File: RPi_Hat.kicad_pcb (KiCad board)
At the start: 2 copper layers, 65 x 56 mm, 29 parts, among them J1 CONN_02X19, J10 CONN_01X04, J2 RPi_GPIO, J3 CONN_02X06, J4 CONN_02X06, J5 CONN_02X06, J6 CONN_02X10, J7 CONN_02X10, J8 CONN_02X10, J9 CONN_01X04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

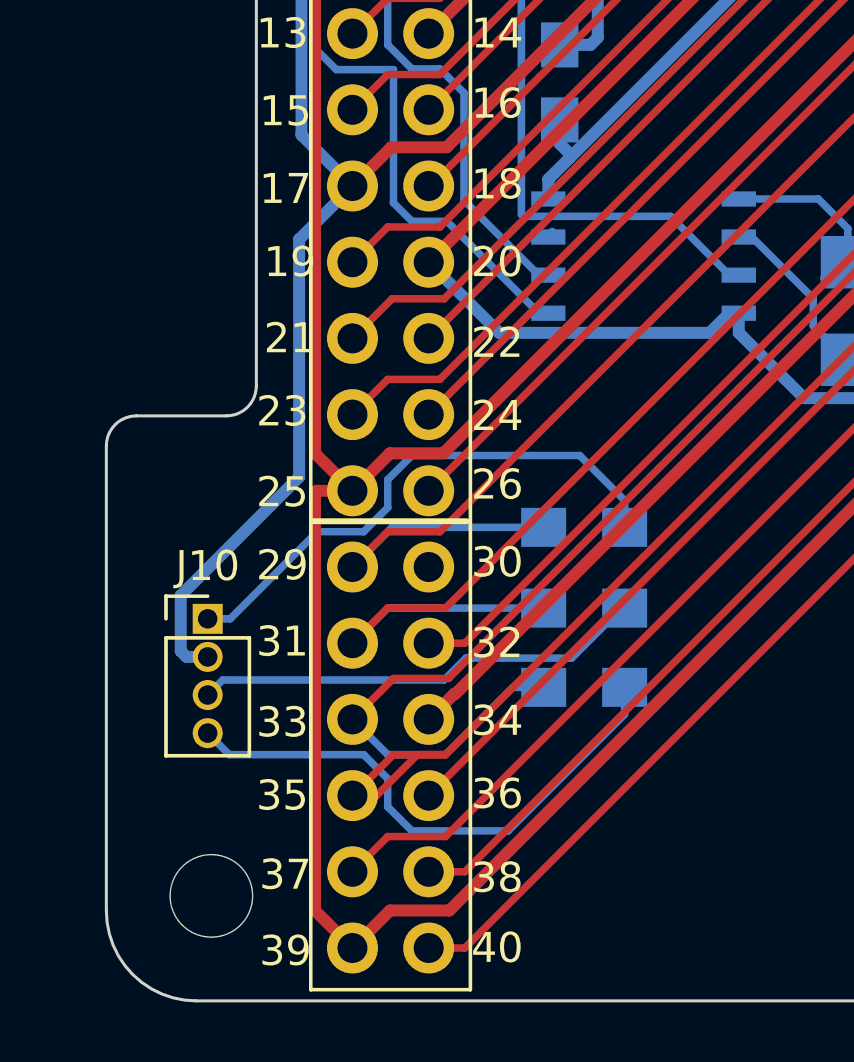
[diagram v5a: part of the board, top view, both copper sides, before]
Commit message: support SMD RGB LED as well
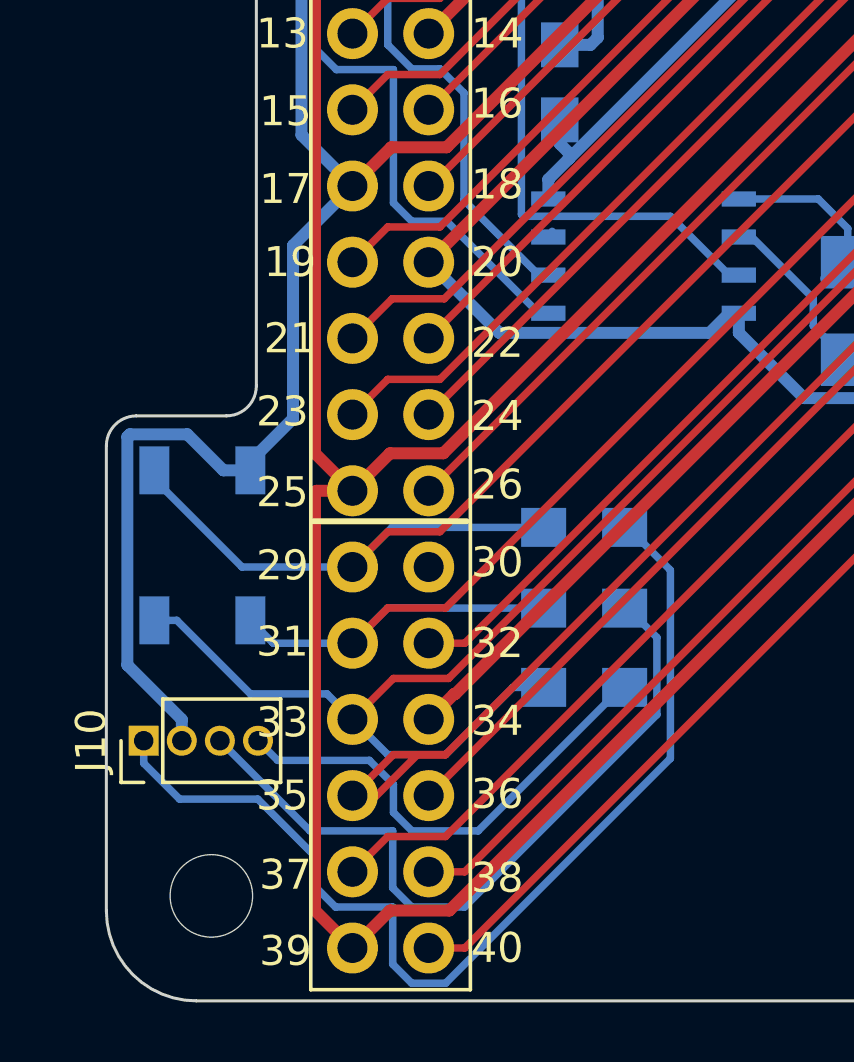
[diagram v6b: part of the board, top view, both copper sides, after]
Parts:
- added D1: LED_RABG, LEDs:LED_WS2812B-PLCC4, B.Cu at (3.20, 41.3)
- moved J10 4.59 mm to (1.24, 47.8), turned to 90 degrees
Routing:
- net Net-(J10-Pad1): track 18.2 -> 34.5 mm
- net Net-(J10-Pad3): track 15.1 -> 24.8 mm
- net Pin29: track 59.5 -> 67.7 mm
- net Pin33: track 67.6 -> 75.6 mm
- net 3.3V: track 204.9 -> 212.4 mm
- net Pin31: track 63.1 -> 66.9 mm
- net Net-(J10-Pad4): track 18.3 -> 16.0 mm

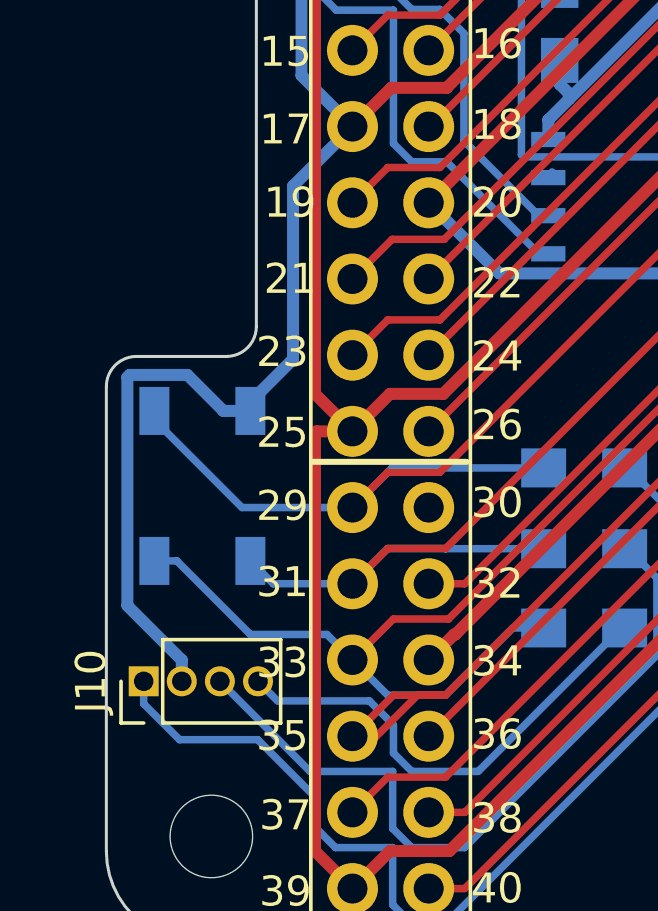
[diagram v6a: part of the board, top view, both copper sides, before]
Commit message: remove SMD LED
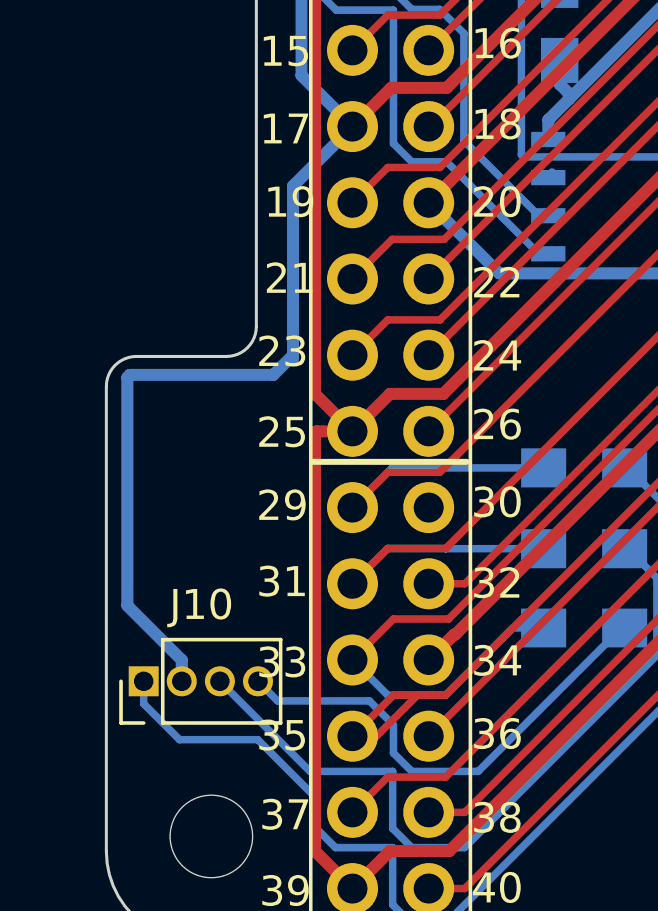
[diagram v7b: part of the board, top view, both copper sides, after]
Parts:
- removed D1: LED_RABG, LEDs:LED_WS2812B-PLCC4
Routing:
- net Pin29: track 67.7 -> 59.6 mm
- net Pin33: track 75.6 -> 67.6 mm
- net Pin31: track 66.9 -> 63.1 mm
- net 3.3V: track 212.4 -> 211.3 mm
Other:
- board text removed: "Select one of these board edges depending upon the type of socket that is used."
